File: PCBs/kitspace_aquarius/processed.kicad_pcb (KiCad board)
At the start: 2 copper layers, 74 x 120 mm, 79 parts, among them J1 Conn_01x04, J2 USB_B_Micro, J3 Conn_01x02, Q1 DTC114E, Q10 DTC114E, Q11 DTC114E, Q12 DTC114E, Q13 DTC114E, Q2 DTC114E, Q3 DTC114E, Q4 DTC114E, Q5 DTC114E, Q6 DTC114E, Q7 DTC114E, Q8 DTC114E, Q9 DTC114E, SW1 SW_DPDT_x2, SW2 SW_Push, U1 TM4C1231C3PM, U2 TPS73633DBV, X1 theGirl, X2 jlcpcb_order, X3 DesignedWithKicad, X4 OpenSourceHardware, X5 choose_indication, X6 control_indication, Y1 16MHz

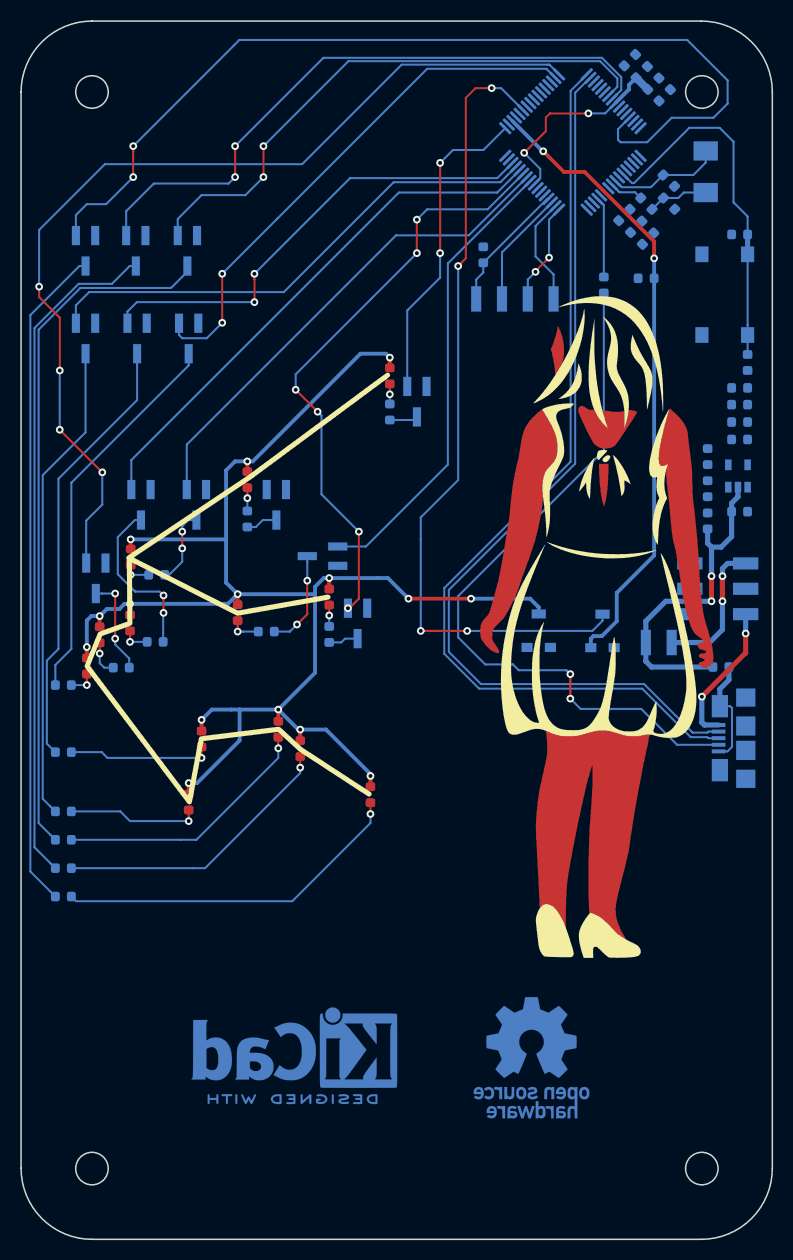
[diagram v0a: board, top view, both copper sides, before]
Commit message: recheck all circuits and clean up fill zone by rerouting the nets using freerouting and manually
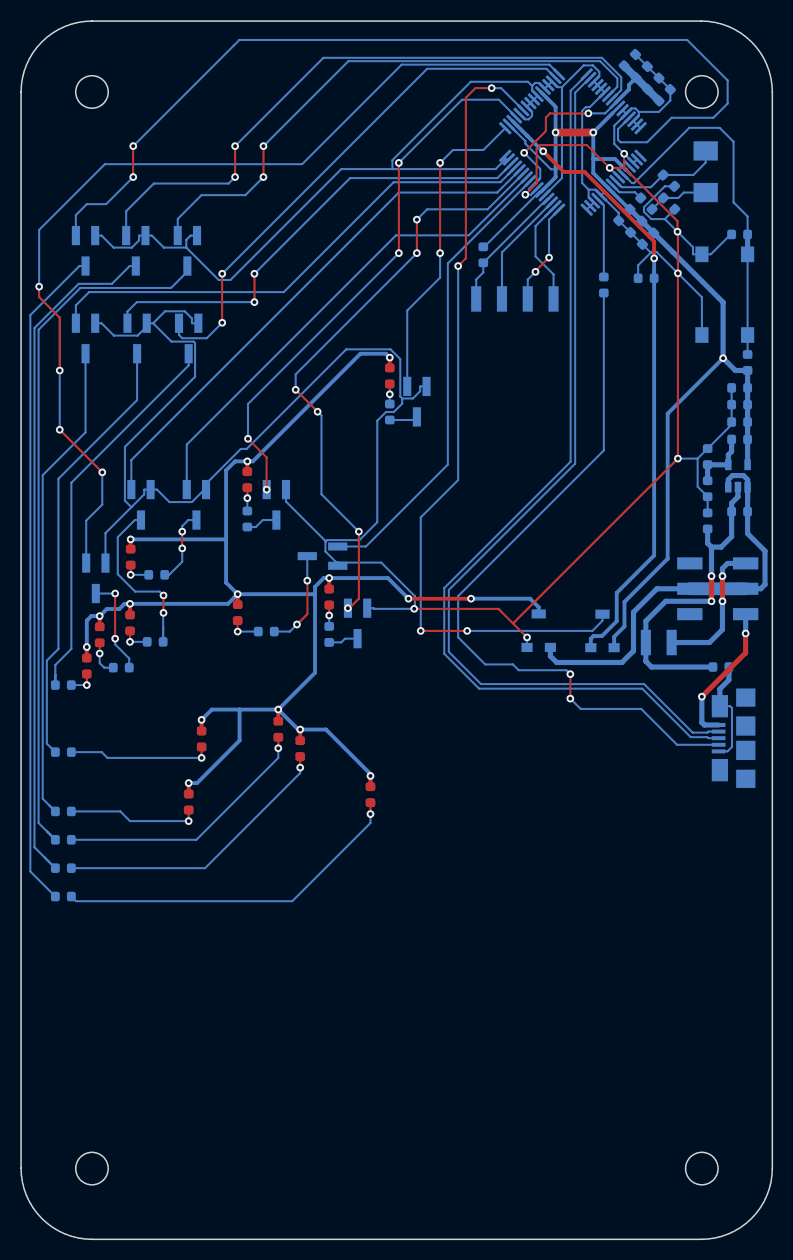
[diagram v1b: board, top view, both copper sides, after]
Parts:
- removed X1: theGirl, aquarius:theGirl
- removed X3: DesignedWithKicad, Symbol:KiCad-Logo2_8mm_Copper
- removed X4: OpenSourceHardware, Symbol:OSHW-Logo_11.4x12mm_Copper
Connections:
- C1 pad 2: (no net) -> GNDD
- C10 pad 1: (no net) -> +3V3
- C10 pad 2: (no net) -> GNDD
- C11 pad 1: (no net) -> +3V3
- C11 pad 2: (no net) -> GNDD
- C12 pad 1: (no net) -> +3V3
- C12 pad 2: (no net) -> GNDD
- C13 pad 1: (no net) -> +3V3
- C13 pad 2: (no net) -> GNDD
- C14 pad 1: (no net) -> +3V3
- C14 pad 2: (no net) -> GNDD
- C15 pad 2: (no net) -> GNDD
- C2 pad 2: (no net) -> GNDD
- C3 pad 1: (no net) -> Net-(C3-Pad1)
- C3 pad 2: (no net) -> GNDD
- C4 pad 1: (no net) -> Net-(C3-Pad1)
- C4 pad 2: (no net) -> GNDD
- C5 pad 2: (no net) -> GNDD
- C6 pad 2: (no net) -> GNDD
- C7 pad 1: (no net) -> VBUS
- C8 pad 1: (no net) -> Net-(C8-Pad1)
- C8 pad 2: (no net) -> GNDD
- C9 pad 1: (no net) -> +3V3
- C9 pad 2: (no net) -> GNDD
- Q1 pad 2: (no net) -> GNDD
- Q10 pad 2: (no net) -> GNDD
- Q11 pad 2: (no net) -> GNDD
- Q12 pad 2: (no net) -> GNDD
- Q13 pad 2: (no net) -> GNDD
- Q2 pad 1: (no net) -> /Leds/Stars/LED1
- Q2 pad 2: (no net) -> GNDD
- Q3 pad 2: (no net) -> GNDD
- Q4 pad 2: (no net) -> GNDD
- Q5 pad 1: (no net) -> /Leds/Stars/LED4
- Q5 pad 2: (no net) -> GNDD
- Q6 pad 2: (no net) -> GNDD
- Q7 pad 2: (no net) -> GNDD
- Q8 pad 2: (no net) -> GNDD
- Q9 pad 2: (no net) -> GNDD
- R19 pad 2: (no net) -> GNDD
- R20 pad 1: (no net) -> GNDD
- R21 pad 1: (no net) -> +3V3
- R21 pad 2: (no net) -> Net-(C8-Pad1)
- R22 pad 1: (no net) -> +3V3
- R23 pad 2: (no net) -> +3V3
- R24 pad 1: (no net) -> Net-(C8-Pad1)
- R24 pad 2: (no net) -> GNDD
- RV1 pad 1: (no net) -> +3V3
- RV2 pad 1: (no net) -> VBUS
- RV2 pad 3: (no net) -> GNDD
- SW1 pad 2: (no net) -> VBUS
- SW1 pad 5: (no net) -> VBUS
- SW2 pad 1: (no net) -> GNDD
- U1 pad 10: (no net) -> GNDD
- U1 pad 11: (no net) -> +3V3
- U1 pad 12: (no net) -> GNDD
- U1 pad 13: (no net) -> GNDD
- U1 pad 14: (no net) -> GNDD
- U1 pad 19: (no net) -> GNDD
- U1 pad 2: (no net) -> +3V3
- U1 pad 20: (no net) -> GNDD
- U1 pad 21: (no net) -> GNDD
- U1 pad 22: (no net) -> GNDD
- U1 pad 26: (no net) -> +3V3
- U1 pad 27: (no net) -> GNDD
- U1 pad 28: (no net) -> GNDD
- U1 pad 30: (no net) -> GNDD
- U1 pad 31: (no net) -> GNDD
- U1 pad 32: (no net) -> GNDD
- U1 pad 34: (no net) -> GNDD
- U1 pad 35: (no net) -> GNDD
- U1 pad 37: (no net) -> +3V3
- U1 pad 39: (no net) -> GNDD
- U1 pad 4: (no net) -> /Leds/Stars/LED1
- U1 pad 42: (no net) -> +3V3
- U1 pad 43: (no net) -> GNDD
- U1 pad 44: (no net) -> GNDD
- U1 pad 46: (no net) -> GNDD
- U1 pad 47: (no net) -> GNDD
- U1 pad 48: (no net) -> GNDD
- U1 pad 5: (no net) -> GNDD
- U1 pad 53: (no net) -> GNDD
- U1 pad 54: (no net) -> +3V3
- U1 pad 55: (no net) -> GNDD
- U1 pad 63: (no net) -> GNDD
- U1 pad 64: (no net) -> GNDD
- U1 pad 7: (no net) -> GNDD
- U1 pad 8: (no net) -> GNDD
- U1 pad 9: (no net) -> GNDD
- U2 pad 1: (no net) -> VBUS
- U2 pad 3: (no net) -> VBUS
- U2 pad 4: (no net) -> Net-(C8-Pad1)
- U2 pad 5: (no net) -> +3V3
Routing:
- net GNDD: track 0.00 -> 403.4 mm, vias 0 -> 8
- net +3V3: track 0.00 -> 110.4 mm, vias 0 -> 3
- net /Leds/Stars/LED1: track 0.00 -> 54.0 mm, vias 0 -> 4
- net VBUS: track 0.00 -> 42.5 mm
- net Net-(C8-Pad1): track 0.00 -> 6.86 mm
- net Net-(C3-Pad1): track 20.8 -> 24.5 mm
- net GNDA: track 61.9 -> 64.8 mm
- net Net-(Q12-Pad3): track 66.6 -> 68.0 mm
- net Net-(Q6-Pad3): track 16.6 -> 18.0 mm
- net /Inputs/TDI: track 10.7 -> 12.1 mm
- net Net-(Q11-Pad3): track 68.5 -> 69.7 mm
- net /Leds/Stars/LED8: track 50.8 -> 51.9 mm
- net /Leds/Stars/LED9: track 46.8 -> 47.8 mm
- net Net-(Q8-Pad3): track 38.1 -> 39.1 mm
- net Net-(Q9-Pad3): track 47.3 -> 48.2 mm
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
